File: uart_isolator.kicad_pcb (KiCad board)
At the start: 2 copper layers, 22.6 x 33.8 mm, 15 parts, among them J1 Conn_01x02_Pin, J2 Conn_01x02_Pin, J3 Conn_01x02_Pin, J4 Conn_01x02_Pin, J5 Conn_01x02_Pin, J6 Conn_01x02_Pin, J7 Conn_01x04_Pin, Q1 BSS123, Q2 BSS123, U1 TLP175A

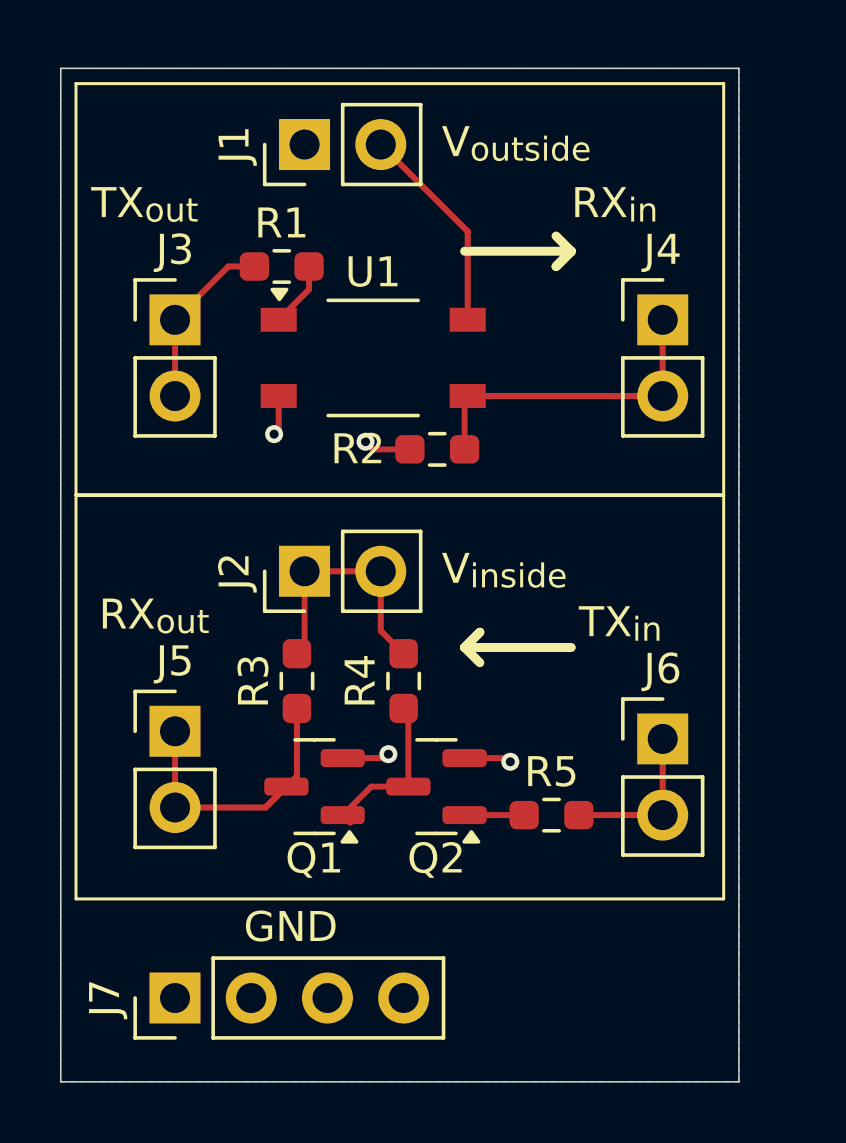
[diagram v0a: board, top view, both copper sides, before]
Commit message: Change to using voltage buffer
 - Silkmask updates to clarify labels
 - Using voltage buffer to isolate TX_in from RX_out
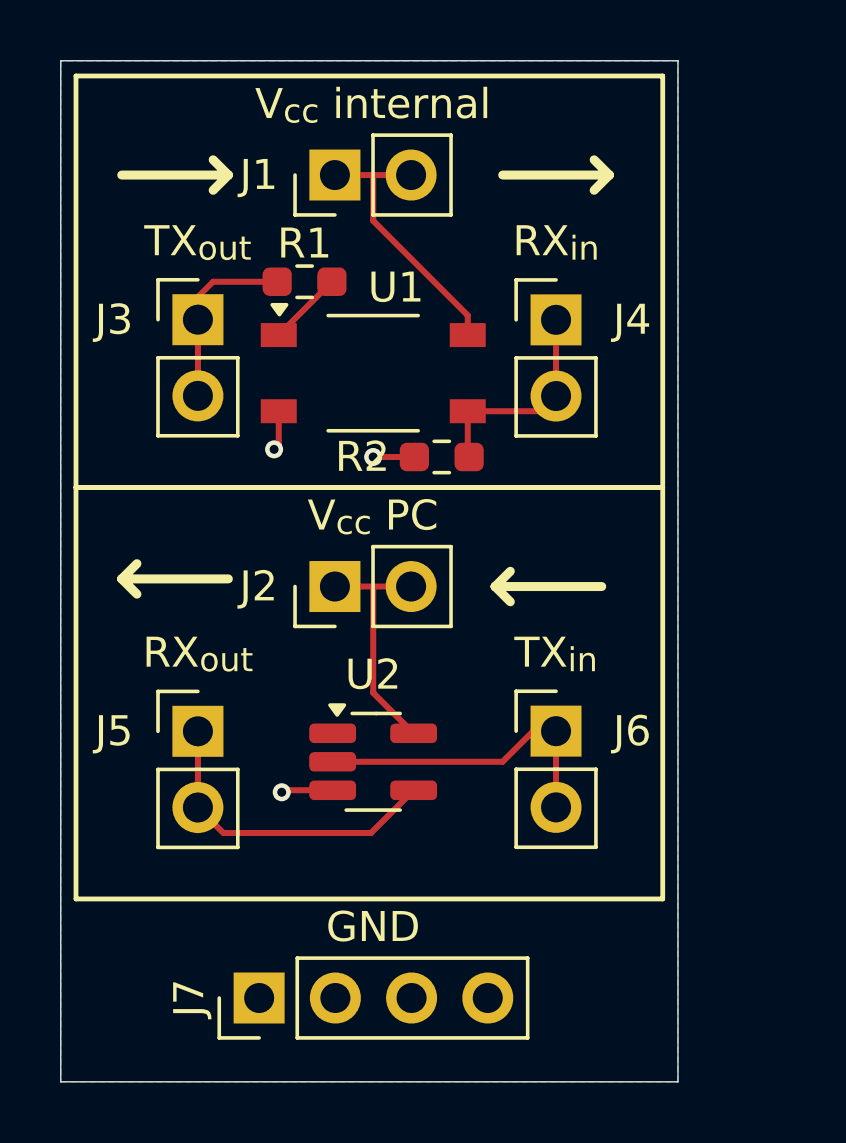
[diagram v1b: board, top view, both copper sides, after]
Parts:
- removed Q1, Q2: BSS123, Package_TO_SOT_SMD:SOT-23
- removed R3, R4, R5: R_US, Resistor_SMD:R_0603_1608Metric_Pad0.98x0.95mm_HandSolder
- added U2: SN74AUP1G34, Package_TO_SOT_SMD:SOT-23-5_HandSoldering, F.Cu at (137.2, 97.0)
- moved J6 3.57 mm to (143.3, 96.0)
- moved J4 3.56 mm to (143.3, 82.3)
- moved J7 2.80 mm to (133.4, 104.9)
- moved J1 1.43 mm to (135.9, 77.5)
- moved J2 1.13 mm to (135.9, 91.2)
- moved R1 0.92 mm to (134.9, 81.0)
- moved J3 0.76 mm to (131.3, 82.3)
- moved J5 0.76 mm to (131.3, 96.0)
- moved U1 0.51 mm to (137.2, 84.1)
- moved R2 0.30 mm to (139.4, 86.9)
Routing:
- net Net-(Q1-G): track 5.61 -> 0.00 mm
- net /internal_tx: track 5.33 -> 10.4 mm
- net /internal_rx: track 10.9 -> 5.95 mm
- net VCC_internal: track 7.19 -> 9.18 mm
- net Net-(Q2-G): track 1.99 -> 0.00 mm
- net GND: track 6.07 -> 4.39 mm, vias 4 -> 3
- net /external_rx: track 9.98 -> 11.4 mm
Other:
- board size 22.6 x 33.8 mm -> 20.6 x 34 mm
- board text added: "JLCJLCJLCJLC"
- board text added: "V_{cc} PC"
- board text added: "V_{cc} internal"
- board text removed: "V_{inside}"
- board text removed: "V_{outside}"

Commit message: Rev A
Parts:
- added C1: 100n, Capacitor_SMD:C_0603_1608Metric_Pad1.08x0.95mm_HandSolder, F.Cu at (96.8, 96.8)
- added C2: 100n, Capacitor_SMD:C_0603_1608Metric_Pad1.08x0.95mm_HandSolder, F.Cu at (99.8, 86.6)
- added C3: 47p, Capacitor_SMD:C_0603_1608Metric_Pad1.08x0.95mm_HandSolder, F.Cu at (88.6, 90.0)
- added C4: 47p, Capacitor_SMD:C_0603_1608Metric_Pad1.08x0.95mm_HandSolder, F.Cu at (88.6, 93.5)
- added C5: 10u, Capacitor_SMD:C_0603_1608Metric_Pad1.08x0.95mm_HandSolder, F.Cu at (88.2, 83.2)
- added C6: 10u, Capacitor_SMD:C_0603_1608Metric_Pad1.08x0.95mm_HandSolder, F.Cu at (95.0, 85.1)
- added D1: LED, LED_SMD:LED_0603_1608Metric_Pad1.05x0.95mm_HandSolder, F.Cu at (93.7, 81.0)
- added D2: LED, LED_SMD:LED_0603_1608Metric_Pad1.05x0.95mm_HandSolder, F.Cu at (112.0, 96.3)
- added D3: LED, LED_SMD:LED_0603_1608Metric_Pad1.05x0.95mm_HandSolder, F.Cu at (112.0, 100.8)
- added H1: MountingHole_Pad, MountingHole:MountingHole_2.2mm_M2_Pad_Via, F.Cu at (80.9, 81.9)
- added H2: MountingHole_Pad, MountingHole:MountingHole_2.2mm_M2_Pad_Via, F.Cu at (93.6, 104.4)
- added H3: MountingHole_Pad, MountingHole:MountingHole_2.2mm_M2_Pad_Via, F.Cu at (114.7, 104.4)
- added J10: Conn_01x02_Pin, Connector_PinHeader_2.54mm:PinHeader_1x02_P2.54mm_Vertical, F.Cu at (105.4, 84.3)
- added J11: Conn_01x02_Pin, Connector_PinHeader_2.54mm:PinHeader_1x02_P2.54mm_Vertical, F.Cu at (105.4, 88.4)
- added J12: USB_C_Receptacle_USB2.0, Marcano:USB4105-GF-A, F.Cu at (81.6, 90.9)
- added J13: Conn_01x02_Pin, Connector_PinHeader_2.54mm:PinHeader_1x02_P2.54mm_Vertical, F.Cu at (105.4, 92.5)
- added J14: Conn_01x02_Pin, Connector_PinHeader_2.54mm:PinHeader_1x02_P2.54mm_Vertical, F.Cu at (105.4, 96.5)
- added J15: Conn_01x02_Pin, Connector_PinHeader_2.54mm:PinHeader_1x02_P2.54mm_Vertical, F.Cu at (105.4, 100.6)
- added J16: Conn_01x02_Pin, Connector_PinHeader_2.54mm:PinHeader_1x02_P2.54mm_Vertical, F.Cu at (105.4, 104.6)
- added J8: Conn_01x02_Pin, Connector_PinHeader_2.54mm:PinHeader_1x02_P2.54mm_Vertical, F.Cu at (105.4, 76.2)
- added J9: Conn_01x02_Pin, Connector_PinHeader_2.54mm:PinHeader_1x02_P2.54mm_Vertical, F.Cu at (105.4, 80.3)
- added R3: 27, Resistor_SMD:R_0603_1608Metric_Pad0.98x0.95mm_HandSolder, F.Cu at (92.4, 91.9)
- added R4: 27, Resistor_SMD:R_0603_1608Metric_Pad0.98x0.95mm_HandSolder, F.Cu at (92.4, 89.2)
- added R5: 5.1k, Resistor_SMD:R_0603_1608Metric_Pad0.98x0.95mm_HandSolder, F.Cu at (86.9, 86.6)
- added R6: 5.1k, Resistor_SMD:R_0603_1608Metric_Pad0.98x0.95mm_HandSolder, F.Cu at (86.9, 95.5)
- added R7: 1k, Resistor_SMD:R_0603_1608Metric_Pad0.98x0.95mm_HandSolder, F.Cu at (93.7, 79.2)
- added R8: 1k, Resistor_SMD:R_0603_1608Metric_Pad0.98x0.95mm_HandSolder, F.Cu at (100.3, 96.5)
- added R9: 1k, Resistor_SMD:R_0603_1608Metric_Pad0.98x0.95mm_HandSolder, F.Cu at (100.3, 99.1)
- added U3: FT230XS, Package_SO:SSOP-16_3.9x4.9mm_P0.635mm, F.Cu at (97.9, 91.2)
- added U4: TLV74033PDBVR, Package_TO_SOT_SMD:SOT-23-5_HandSoldering, F.Cu at (91.4, 85.0)
- R1: value R_US -> 1k
- R2: value R_US -> 95.3k
- moved J3 13.2 mm to (118.1, 82.5)
- moved J5 13.2 mm to (118.1, 96.3)
- moved J7 13.2 mm to (120.2, 105.2)
- moved J4 13.2 mm to (130.0, 82.5)
- moved J6 13.2 mm to (130.0, 96.3)
- moved R1 13.2 mm to (121.7, 81.3)
- moved R2 13.2 mm to (126.2, 87.1)
- moved U1 13.2 mm to (124.0, 84.3)
- moved U2 13.2 mm to (124.0, 97.3)
- moved J1 13.2 mm to (122.7, 77.7)
- moved J2 13.2 mm to (122.7, 91.4)
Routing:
- net VCC_external: track 7.99 -> 86.2 mm, vias 0 -> 4
- net Net-(J16-Pin_1): track 0.00 -> 20.5 mm
- net /external_rx: track 11.4 -> 31.6 mm
- net /VBUS_5V: track 0.00 -> 20.2 mm
- net GND: track 4.39 -> 23.3 mm, vias 3 -> 17
- net Net-(J8-Pin_1): track 0.00 -> 16.7 mm, vias 0 -> 4
- net Net-(U3-CBUS2): track 0.00 -> 14.5 mm
- net Net-(J9-Pin_1): track 0.00 -> 13.6 mm, vias 0 -> 2
- net /external_tx: track 6.15 -> 18.9 mm
- net Net-(J11-Pin_1): track 0.00 -> 12.4 mm
- net Net-(J13-Pin_1): track 0.00 -> 11.4 mm, vias 0 -> 2
- net /USBDP: track 0.00 -> 10.8 mm, vias 0 -> 2
- net Net-(J10-Pin_1): track 0.00 -> 10.6 mm
- net Net-(D3-K): track 0.00 -> 9.77 mm
- net /USBDM: track 0.00 -> 9.35 mm
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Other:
- board size 20.6 x 34 mm -> 57.4 x 33.8 mm
- board text added: "${AUTHOR} ${COMPANY} ${ISSUE_DATE} REV: ${REVISION}"
- board text added: "${TITLE} 3.3V"
- board text added: "3.3V LED"
- board text added: "CBUS0 CBUS1 CBUS2 CBUS3"
- board text added: "RX"
- board text added: "TX"
- board text added: "TX(J) RX(J) ~{RTS} ~{CTS}"
- board text added: "V_{3.3} PC (output)"
- board text added: "V_{cc} internal (input)"
- board text removed: "V_{cc} PC"
- board text removed: "V_{cc} internal"
